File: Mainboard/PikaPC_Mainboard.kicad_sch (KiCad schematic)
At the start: 73 parts, among them J1 Conn_02x20_Odd_Even, J10 Conn_01x08, J11 Conn_01x08, J12 Conn_01x08, J13 Conn_01x08, J14 Conn_01x08, J15 Conn_01x08, J16 Conn_01x08, J17 Conn_01x08, J18 Conn_01x10, J19 Conn_02x05_Odd_Even, J2 Conn_02x20_Odd_Even, J3 Conn_02x20_Odd_Even, J4 Conn_02x20_Odd_Even, J5 DIN41612_03x32_C_Split, J6 Mini-DIN-6, J7 Mini-DIN-6, J9 Conn_01x08, SW1 SW_Push_DPDT, SW2 SW_Push, U1 PPC403GA, U10 74LS07, U12 GD75232N, U13 74LVC125, U14 MCP120-315GI/TO, U15 AS6C4008-55PCN, U16 AS6C4008-55PCN, U2 SN74LVC245A, U3 SST39VF010, U4 SN74LVC245A, U5 SN74LVC245A, U6 SN74LVC245A, U7 8042 PS/2, U8 ATF22V10C, U9 74LS04, Y1 25M, Y2 7M3728, Y3 14M31818

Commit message: Add vS3 ViRGE video & SD interface
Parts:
- removed J1, J2, J3, J4: Conn_02x20_Odd_Even, Connector_PinHeader_2.54mm:PinHeader_2x20_P2.54mm_Vertical, symbol Connector_Generic:Conn_02x20_Odd_Even
- added C24: 100nF, Capacitor_THT:C_Disc_D3.0mm_W2.0mm_P2.50mm, symbol Device:C_Small_US
- added J1: Conn_02x05_Odd_Even, Connector_PinHeader_2.54mm:PinHeader_2x05_P2.54mm_Vertical, symbol Connector_Generic:Conn_02x05_Odd_Even
- added J8: Conn_01x06, Connector_PinHeader_2.54mm:PinHeader_1x06_P2.54mm_Vertical, symbol Connector_Generic:Conn_01x06
- added R11, R6, R7: 75R, Resistor_THT:R_Axial_DIN0204_L3.6mm_D1.6mm_P2.54mm_Vertical, symbol Device:R_Small_US
- added R12, R13, R14, R15, R16: 10k, Resistor_THT:R_Axial_DIN0204_L3.6mm_D1.6mm_P2.54mm_Vertical, symbol Device:R_Small_US
- added R3: 4k7, Resistor_THT:R_Axial_DIN0204_L3.6mm_D1.6mm_P2.54mm_Vertical, symbol Device:R_Small_US
- added R4: 147R, Resistor_THT:R_Axial_DIN0204_L3.6mm_D1.6mm_P2.54mm_Vertical, symbol Device:R_Small_US
- added U11: 86C325, Package_QFP:PQFP-208_28x28mm_P0.5mm, symbol PikaPC:S3 86C325 ViRGE
- added U17: ATF1504, Package_LCC:PLCC-44_THT-Socket, symbol Wrap030-ATX:ATF1504AS
- added U18, U19, U20, U21: T224162B, Package_SO:SOJ-44_10.16x28.575mm_P1.27mm, symbol PikaPC:T224162B-xJ
- C19, C20, C21, C22: footprint Capacitor_THT:C_Disc_D7.5mm_W5.0mm_P7.50mm -> Capacitor_THT:C_Disc_D3.0mm_W2.0mm_P2.50mm
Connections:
- net +3.3V: now also U13.2, U13.5
- net +5V: now also J8.5 (Pin_5), R3.2, U11.12 (Vdd), U11.137 (Vdd), U11.158 (CLKAVdd1), U11.160 (CLKAVdd2), U11.164 (AVdd), U11.165 (~{PDOWN}), U11.169 (AVdd), U11.170 (AVdd), U11.192 (Vdd), U11.37 (Vdd), U11.62 (Vdd), U11.81 (Vdd), U11.96 (Vdd), U17.15 (VCC), U17.23 (VCC), U17.35 (VCC), U18.1 (Vcc), U18.20 (Vcc), U18.6 (Vcc), U19.1 (Vcc), U19.20 (Vcc), U19.6 (Vcc), U20.1 (Vcc), U20.20 (Vcc), U20.6 (Vcc), U21.1 (Vcc), U21.20 (Vcc), U21.6 (Vcc)
- net A10: now also U11.185 (SA10)
- net A11: now also U11.186 (SA11)
- net A12: now also U11.187 (SA12)
- net A13: now also U11.188 (SA13)
- net A14: now also U11.189 (SA14)
- net A15: now also U11.190 (SA15)
- net A16: now also U11.191 (SA16)
- net A17: now also U11.196 (SA17)
- net A18: now also U11.197 (SA18)
- net A19: now also U11.198 (SA19)
- net A2: now also U11.176 (SA2)
- net A20: now also U11.199 (SA20)
- net A21: now also U11.200 (SA21)
- net A22: now also U11.201 (SA22)
- net A3: now also U11.177 (SA3)
- net A4: now also U11.178 (SA4)
- net A5: now also U11.179 (SA5)
- net A6: now also U11.180 (SA6)
- net A7: now also U11.181 (SA7)
- net A8: now also U11.182 (SA8)
- net A9: now also U11.183 (SA9)
- net GND: now also C24.2, J1.10 (Pin_10), J1.2 (Pin_2), J1.4 (Pin_4), J1.6 (Pin_6), J1.8 (Pin_8), J8.6 (Pin_6), R11.2, R12.2, R13.2, R14.2, R15.2, R16.2, R4.2, R6.2, R7.2, U11.114 (Vss), U11.123 (Vss), U11.126 (Vss), U11.135 (Vss), U11.145 (Vss), U11.159 (AVss), U11.161 (AVss), U11.163 (Vss), U11.167 (AVss), U11.173 (AVss), U11.195 (Vss), U11.22 (Vss), U11.32 (Vss), U11.47 (Vss), U11.60 (Vss), U11.71 (Vss), U11.87 (Vss), U11.9 (Vss), U11.99 (Vss), U17.10 (GND), U17.22 (GND), U17.30 (GND), U17.42 (GND), U18.21 (Vss), U18.35 (Vss), U18.40 (Vss), U19.21 (Vss), U19.35 (Vss), U19.40 (Vss), U20.21 (Vss), U20.35 (Vss), U20.40 (Vss), U21.21 (Vss), U21.35 (Vss), U21.40 (Vss); no longer U13.1, U13.4
- net INT0: now also U11.152 (SINTR)
- net INT1: now also U17.17 (IO24)
- net PD0: now also U11.46 (SD0)
- net PD1: now also R12.1, U11.45 (SD1)
- net PD10: now also U11.34 (SD10)
- net PD11: now also U11.33 (SD11)
- net PD12: now also U11.31 (SD12)
- net PD13: now also U11.30 (SD13)
- net PD14: now also U11.29 (SD14)
- net PD15: now also U11.28 (SD15)
- net PD16: now also U11.18 (SD16)
- net PD17: now also U11.17 (SD17)
- net PD18: now also U11.16 (SD18)
- net PD19: now also U11.15 (SD19)
- net PD2: now also R13.1, U11.44 (SD2)
- net PD20: now also U11.14 (SD20)
- net PD21: now also U11.13 (SD21)
- net PD22: now also U11.11 (SD22)
- net PD23: now also U11.10 (SD23)
- net PD24: now also U11.6 (SD24), U17.8 (IO5)
- net PD25: now also U11.5 (SD25), U17.6 (IO11)
- net PD26: now also U11.4 (SD26), U17.5 (IO14)
- net PD27: now also U11.3 (SD27), U17.4 (IO16)
- net PD28: now also U11.2 (SD28), U17.21 (IO17)
- net PD29: now also U11.1 (SD29), U17.20 (IO19)
- net PD3: now also U11.43 (SD3)
- net PD30: now also U11.208 (SD30), U17.19 (IO20)
- net PD31: now also U11.207 (SD31), U17.18 (IO21)
- net PD4: now also R14.1, U11.42 (SD4)
- net PD5: now also R15.1, U11.41 (SD5)
- net PD6: now also R16.1, U11.40 (SD6)
- net PD7: now also U11.39 (SD7)
- net PD8: now also U11.36 (SD8)
- net PD9: now also U11.35 (SD9)
- net Ready: now also U13.3, U13.6; no longer U8.22 (IO22)
- net R/~{W}: now also U17.11 (IO3)
- net SysClk-5v: now also U11.194 (SCLK), U17.43 (GCLK1)
- net VidClk: now also U11.156 (XIN)
- net ~{CS2}: now also U11.50 (SAUP2)
- net ~{CS3}: now also U11.25 (SAUP1), U11.8 (SM/~{IO})
- net ~{CS4}: now also U17.9 (IO4)
- net ~{OE}: now also U11.26 (SW/~{R})
- net ~{Reset}: now also U10.11, U17.1 (GCLR)
- net ~{VID-ADS}: now also U11.20 (~{SADS})
- net ~{VID-RDYIN}: now also U11.21 (~{RDYIN})
- net ~{VID-SBE0}: now also U11.38 (~{SBE0})
- net ~{VID-SBE1}: now also U11.27 (~{SBE1})
- net ~{VID-SBE2}: now also U11.19 (~{SBE2})
- net ~{VID-SBE3}: now also U11.7 (~{SBE3})
- net ~{VID-SRDYn}: now also U11.23 (~{SRDY})
- net MSCO: now reaches U7.24 (MSCO), U9.3
- net ~{MSCO}: now reaches U10.3, U9.4
- net KBCO: now reaches U7.37 (KBCO), U9.5
- net ~{KBCO}: now reaches U10.5, U9.6
- net ~{KBDO}: now reaches U10.9, U9.8
- net KBDO: now reaches U7.38 (KBDO), U9.9
- net ~{MSDO}: now reaches U10.1, U9.2
- net ~{Reset-5v}: now reaches U10.10
- net ~{Reset-5v}: now also R3.1, U11.193 (~{SRESET})
- net ~{KINH}: now reaches R10.1, U7.34 (~{KBD-INH})
- net MSDO: now reaches U7.23 (MSDO), U9.1
- new net PDReady: U13.1
- new net RSET: R4.1, U11.166 (RSET)
- new net Ready-5v: U8.22 (IO22)
- new net SDCS: J8.1 (Pin_1), U17.37 (IO53)
- new net SDMISO: J8.4 (Pin_4), U17.41 (IO64)
- new net SDMOSI: J8.3 (Pin_3), U17.40 (IO62)
- new net SDReady: U13.4, U17.12 (IO1)
- new net SDSCK: J8.2 (Pin_2), U17.39 (IO57)
- new net VMA0: U11.79 (MA0), U18.16 (A0), U19.16 (A0), U20.16 (A0), U21.16 (A0)
- new net VMA1: U11.77 (MA1), U18.17 (A1), U19.17 (A1), U20.17 (A1), U21.17 (A1)
- new net VMA2: U11.75 (MA2), U18.18 (A2), U19.18 (A2), U20.18 (A2), U21.18 (A2)
- new net VMA3: U11.73 (MA3), U18.19 (A3), U19.19 (A3), U20.19 (A3), U21.19 (A3)
- new net VMA4: U11.72 (MA4), U18.22 (A4), U19.22 (A4), U20.22 (A4), U21.22 (A4)
- new net VMA5: U11.74 (MA5), U18.23 (A5), U19.23 (A5), U20.23 (A5), U21.23 (A5)
- new net VMA6: U11.76 (MA6), U18.24 (A6), U19.24 (A6), U20.24 (A6), U21.24 (A6)
- new net VMA7: U11.78 (MA7), U18.25 (A7), U19.25 (A7), U20.25 (A7), U21.25 (A7)
- new net VMA8: U11.80 (MA8), U18.26 (A8), U19.26 (A8), U20.26 (A8), U21.26 (A8)
- new net VMD0: U11.104 (PD0), U18.2 (D0)
- new net VMD1: U11.102 (PD1), U18.3 (D1)
- new net VMD10: U11.93 (PD10), U18.33 (D10)
- new net VMD11: U11.95 (PD11), U18.34 (D11)
- new net VMD12: U11.98 (PD12), U18.36 (D12)
- new net VMD13: U11.101 (PD13), U18.37 (D13)
- new net VMD14: U11.103 (PD14), U18.38 (D14)
- new net VMD15: U11.105 (PD15), U18.39 (D15)
- new net VMD16: U11.69 (PD16), U20.2 (D0)
- new net VMD17: U11.67 (PD17), U20.3 (D1)
- new net VMD18: U11.65 (PD18), U20.4 (D2)
- new net VMD19: U11.63 (PD19), U20.5 (D3)
- new net VMD2: U11.100 (PD2), U18.4 (D2)
- new net VMD20: U11.59 (PD20), U20.7 (D4)
- new net VMD21: U11.57 (PD21), U20.8 (D5)
- new net VMD22: U11.55 (PD22), U20.9 (D6)
- new net VMD23: U11.53 (PD23), U20.10 (D7)
- new net VMD24: U11.54 (PD24), U20.31 (D8)
- new net VMD25: U11.56 (PD25), U20.32 (D9)
- new net VMD26: U11.58 (PD26), U20.33 (D10)
- new net VMD27: U11.61 (PD27), U20.34 (D11)
- new net VMD28: U11.64 (PD28), U20.36 (D12)
- new net VMD29: U11.66 (PD29), U20.37 (D13)
- new net VMD3: U11.97 (PD3), U18.5 (D3)
- new net VMD30: U11.68 (PD30), U20.38 (D14)
- new net VMD31: U11.70 (PD31), U20.39 (D15)
- new net VMD32: U11.143 (PD32), U19.2 (D0)
- new net VMD33: U11.141 (PD33), U19.3 (D1)
- new net VMD34: U11.139 (PD34), U19.4 (D2)
- new net VMD35: U11.136 (PD35), U19.5 (D3)
- new net VMD36: U11.133 (PD36), U19.7 (D4)
- new net VMD37: U11.131 (PD37), U19.8 (D5)
- new net VMD38: U11.129 (PD38), U19.9 (D6)
- new net VMD39: U11.127 (PD39), U19.10 (D7)
- new net VMD4: U11.94 (PD4), U18.7 (D4)
- new net VMD40: U11.128 (PD40), U19.31 (D8)
- new net VMD41: U11.130 (PD41), U19.32 (D9)
- new net VMD42: U11.132 (PD42), U19.33 (D10)
- new net VMD43: U11.134 (PD43), U19.34 (D11)
- new net VMD44: U11.138 (PD44), U19.36 (D12)
- new net VMD45: U11.140 (PD45), U19.37 (D13)
- new net VMD46: U11.142 (PD46), U19.38 (D14)
- new net VMD47: U11.144 (PD47), U19.39 (D15)
- new net VMD48: U11.121 (PD48), U21.2 (D0)
- new net VMD49: U11.119 (PD49), U21.3 (D1)
- new net VMD5: U11.92 (PD5), U18.8 (D5)
- new net VMD50: U11.117 (PD50), U21.4 (D2)
- new net VMD51: U11.115 (PD51), U21.5 (D3)
- new net VMD52: U11.112 (PD52), U21.7 (D4)
- new net VMD53: U11.110 (PD53), U21.8 (D5)
- new net VMD54: U11.108 (PD54), U21.9 (D6)
- new net VMD55: U11.106 (PD55), U21.10 (D7)
- new net VMD56: U11.107 (PD56), U21.31 (D8)
- new net VMD57: U11.109 (PD57), U21.32 (D9)
- new net VMD58: U11.111 (PD58), U21.33 (D10)
- new net VMD59: U11.113 (PD59), U21.34 (D11)
- new net VMD6: U11.90 (PD6), U18.9 (D6)
- new net VMD60: U11.116 (PD60), U21.36 (D12)
- new net VMD61: U11.118 (PD61), U21.37 (D13)
- new net VMD62: U11.120 (PD62), U21.38 (D14)
- new net VMD63: U11.122 (PD63), U21.39 (D15)
- new net VMD7: U11.88 (PD7), U18.10 (D7)
- new net VMD8: U11.89 (PD8), U18.31 (D8)
- new net VMD9: U11.91 (PD9), U18.32 (D9)
- new net VREF: C24.1, U11.162 (VREF)
- new net Vid-B: J1.5 (Pin_5), R11.1, U11.172 (AB)
- new net Vid-G: J1.3 (Pin_3), R7.1, U11.171 (AG)
- new net Vid-H: J1.7 (Pin_7), U11.149 (HSYNC)
- new net Vid-R: J1.1 (Pin_1), R6.1, U11.168 (AR)
- new net Vid-V: J1.9 (Pin_9), U11.150 (VSYNC)
- new net ~{VMCAS0}: U11.86 (~{CAS0}), U18.29 (~{CASL})
- new net ~{VMCAS1}: U11.85 (~{CAS1}), U18.28 (~{CASH})
- new net ~{VMCAS2}: U11.82 (~{CAS3}), U20.29 (~{CASL})
- new net ~{VMCAS3}: U11.83 (~{CAS2}), U20.28 (~{CASH})
- new net ~{VMCAS4}: U11.48 (~{CAS4}), U19.29 (~{CASL})
- new net ~{VMCAS5}: U11.49 (~{CAS5}), U19.28 (~{CASH})
- new net ~{VMCAS6}: U11.51 (~{CAS6}), U21.29 (~{CASL})
- new net ~{VMCAS7}: U11.52 (~{CAS7}), U21.28 (~{CASH})
- new net ~{VMOE}: U11.124 (~{OE0}), U18.27 (~{OE}), U19.27 (~{OE}), U20.27 (~{OE}), U21.27 (~{OE})
- new net ~{VMRAS0}: U11.84 (~{RAS0}), U18.14 (~{RAS}), U19.14 (~{RAS}), U20.14 (~{RAS}), U21.14 (~{RAS})
- new net ~{VMWE}: U11.125 (~{WE}), U18.13 (~{WE}), U19.13 (~{WE}), U20.13 (~{WE}), U21.13 (~{WE})
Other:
- moved on the sheet: C19, C20, C21, C22, J6, J7, R10, R2, R5, R8, R9, U10A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

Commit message: cleanup keyboard logic
- odds & ends found while wiring
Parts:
- removed R10, R3: 4k7, Resistor_THT:R_Axial_DIN0204_L3.6mm_D1.6mm_P2.54mm_Vertical, symbol Device:R_Small_US
- removed R2, R5, R8, R9: 10k, Resistor_THT:R_Axial_DIN0204_L3.6mm_D1.6mm_P2.54mm_Vertical, symbol Device:R_Small_US
- added RN4: 9A103J, Resistor_THT:R_Array_SIP9, symbol Device:R_Network08_US
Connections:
- net Ready-5v is gone; now on net PDReady: U8.22 (IO22)
- net +5V: now also RN4.1 (common)
- net KCLK: now also RN4.3 (R2)
- net KDAT: now also RN4.2 (R1)
- net MCLK: now also RN4.5 (R4)
- net MDAT: now also RN4.4 (R3)
- net PDReady: no longer U13.1
- net ~{KINH}: now also RN4.6 (R5)
- net ~{Reset}: now also U11.193 (~{SRESET}); no longer U10.11
- net ~{VID-ADS}: now also U8.16 (IO16); no longer U8.15 (IO15)
- net ~{VID-SBE0}: now also U8.17 (IO17); no longer U8.20 (IO20)
- net ~{VID-SBE1}: now also U8.18 (IO18); no longer U8.19 (IO19)
- net ~{VID-SBE2}: now also U8.19 (IO19); no longer U8.18 (IO18)
- net ~{VID-SBE3}: now also U8.20 (IO20); no longer U8.17 (IO17)
- net ~{VID-SRDYn}: now also U13.1
- net SDReady renamed ~{SDReady}
- net ~{Reset-5v}: no longer names the net of U10.10
- net ~{Reset-5v}: no longer U11.193 (~{SRESET})
- no-connect marks 1 -> 2
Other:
- note added: "ADS-Q1"
- moved on the sheet: C20, C21, U10E

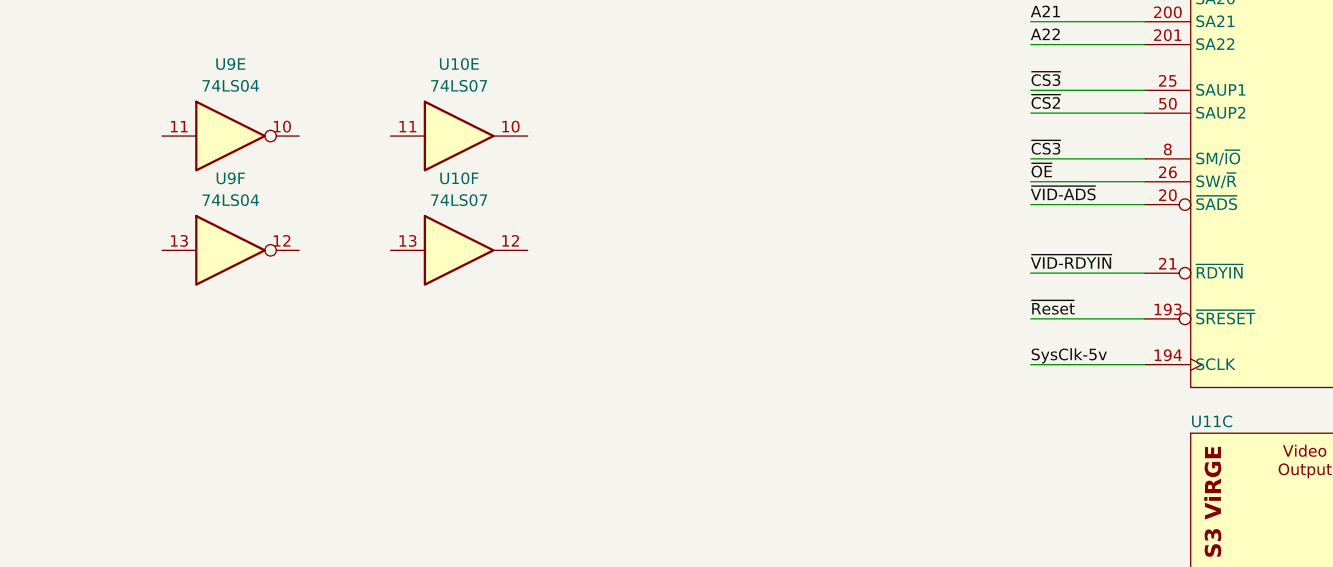
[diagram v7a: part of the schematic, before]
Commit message: Invert system clock to ViRGE
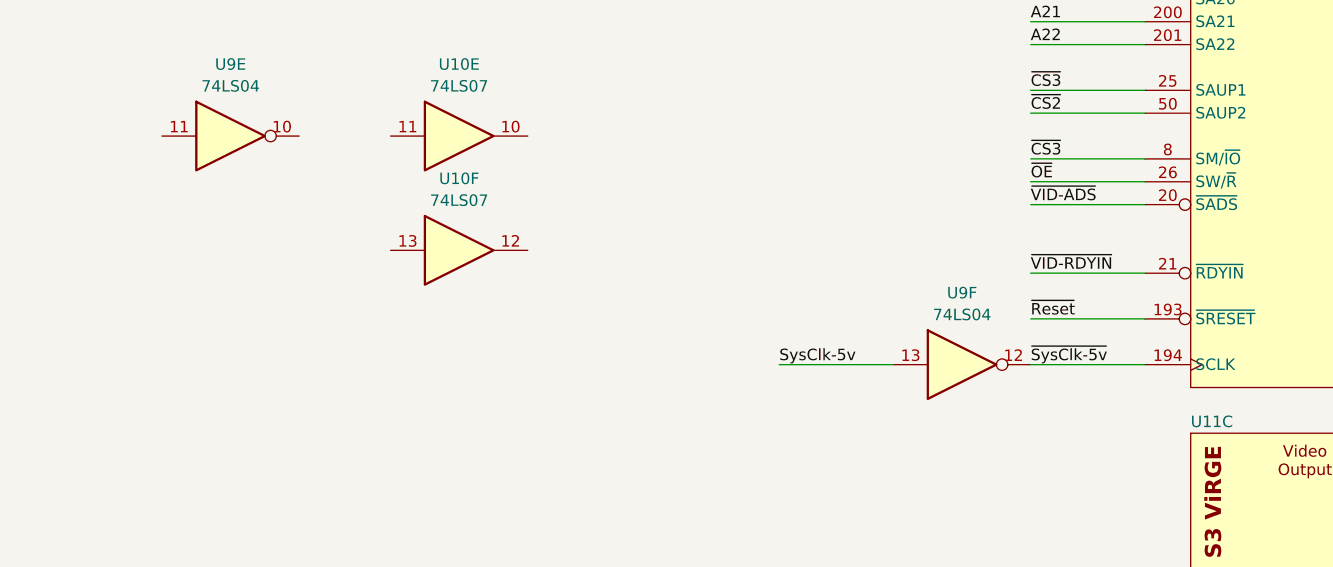
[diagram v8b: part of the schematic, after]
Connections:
- net SysClk-5v: now also U9.13; no longer U11.194 (SCLK)
- net ~{SysClk-5v}: now reaches U9.12
- net ~{SysClk-5v}: now also U11.194 (SCLK)
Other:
- moved on the sheet: U9F
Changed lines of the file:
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@@
 	(wire
 		(pts
+			(xy 906.78 228.6) (xy 919.48 228.6)
+		)
+		(stroke
+			(width 0)
+			(type default)
+		)
+	)
+	(wire
+		(pts
 			(xy 175.26 205.74) (xy 175.26 208.28)
 		)
@@
 		)
 	)
+	(label "SysClk-5v"
+		(at 906.78 228.6 0)
+		(effects
+			(font
+				(size 1.27 1.27)
+			)
+			(justify left bottom)
+		)
+	)
 	(label "PD18"
 		(at 995.68 175.26 180)
@@
 		)
 	)
-	(label "SysClk-5v"
+	(label "~{SysClk-5v}"
 		(at 934.72 228.6 0)
 		(effects
@@
 	(symbol
 		(lib_id "74xx:74LS04")
-		(at 845.82 215.9 0)
+		(at 927.1 228.6 0)
 		(unit 6)
 		(exclude_from_sim no)
@@
 		(fields_autoplaced yes)
 		(property "Reference" "U9"
-			(at 845.82 207.9455 0)
+			(at 927.1 220.6455 0)
 			(effects
 				(font
@@
 		)
 		(property "Value" "74LS04"
-			(at 845.82 210.3698 0)
+			(at 927.1 223.0698 0)
 			(effects
 				(font
@@
 		)
 		(property "Footprint" "Package_DIP:DIP-14_W7.62mm_Socket"
-			(at 845.82 215.9 0)
+			(at 927.1 228.6 0)
 			(effects
 				(font
@@
 		)
 		(property "Datasheet" "http://www.ti.com/lit/gpn/sn74LS04"
-			(at 845.82 215.9 0)
+			(at 927.1 228.6 0)
 			(effects
 				(font
@@
 		)
 		(property "Description" "Hex Inverter"
-			(at 845.82 215.9 0)
+			(at 927.1 228.6 0)
 			(effects
 				(font
